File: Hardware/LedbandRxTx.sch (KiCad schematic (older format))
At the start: 74 parts, among them Q1 LED_RGB 5050, SW1 BUTTON, SW2 BUTTON, SW3 BUTTON, SW4 BUTTON, SW5 SWITCH, SW6 DIPx4

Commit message: PCB routing started. Antenna under construction
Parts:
- removed SW5: SWITCH, BtnsSwitches:SW_SS9, symbol SWITCH
- added SW5: SWITCH_H, symbol SWITCH_H
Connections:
- net +BATT: now also SW5.1
- net BAT_IN: now also SW5.2
- net GND: now also SW5.H
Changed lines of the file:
@@
 Entry Wire Line
 	6350 3100 6450 3200
-$Comp
-L SWITCH SW5
-U 1 1 5528A9A9
-P 3800 10300
-F 0 "SW5" H 3550 10550 60  0000 C CNN
-F 1 "SWITCH" H 3900 10550 60  0000 C CNN
-F 2 "BtnsSwitches:SW_SS9" H 3800 10300 60  0001 C CNN
-F 3 "" H 3800 10300 60  0000 C CNN
-	1    3800 10300
-	1    0    0    -1
-$EndComp
 NoConn ~ 4050 10200
 Text Label 2650 2000 0    60   ~ 0
@@
 Wire Wire Line
 	2100 10050 2100 9600
+$Comp
+L SWITCH_H SW5
+U 1 1 55E2F23F
+P 3800 10300
+F 0 "SW5" H 3550 10550 60  0000 C CNN
+F 1 "SWITCH_H" H 3900 10550 60  0000 C CNN
+F 2 "" H 3800 10300 60  0000 C CNN
+F 3 "" H 3800 10300 60  0000 C CNN
+	1    3800 10300
+	1    0    0    -1
+$EndComp
+$Comp
+L GND #PWR?
+U 1 1 55E2F354
+P 3750 10600
+F 0 "#PWR?" H 3840 10580 30  0001 C CNN
+F 1 "GND" H 3750 10520 30  0001 C CNN
+F 2 "" H 3750 10600 60  0001 C CNN
+F 3 "" H 3750 10600 60  0001 C CNN
+	1    3750 10600
+	1    0    0    -1
+$EndComp
+Wire Wire Line
+	3750 10500 3750 10600
 $EndSCHEMATC

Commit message: + PCB is ready, sent to production
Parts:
- removed XL5: CONN_2, Connectors:TermiBlockHeader_508_x2_R, symbol CONN_2
- added R10, R11: 100k, Resistors:RES_0603, symbol R
- added XL5: CONN_3, Connectors:TermiBlockHeader_508_x3_R, symbol CONN_3
- ANT1: footprint Radio:ANT_868_MEANDER_SALEM -> Radio:ANT_INVF_LEDBANDRXTX
- SW5: footprint (none) -> BtnsSwitches:SW_SS9
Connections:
- net +BATT: now also R10.1
- net Ch1_OUT: now also XL5.1 (P1)
- net GND: now also R11.2, XL5.2 (PM)
- net DataIn: now reaches DD1.10 (ADC0/T2C1ETR/WKUP/PA0)
- net DataIn: now also XL5.3
- net BatMeas: now reaches DD1.11 (ADC1/T2C2/PA1)
- net BatMeas: now also R10.2, R11.1
- no-connect marks 15 -> 13
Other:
- note added: "For WS2812-based band"
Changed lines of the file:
@@
 Text Notes 1900 3050 2    60   ~ 0
 Just\nPins
-NoConn ~ 5750 1700
 $Comp
 L GND #PWR027
@@
 F 0 "ANT1" H 13950 2150 60  0000 C CNN
 F 1 "ANT_PCB_MONO_2PIN" H 14300 2050 60  0000 C CNN
-F 2 "Radio:ANT_868_MEANDER_SALEM" H 14150 1900 60  0001 C CNN
+F 2 "Radio:ANT_INVF_LEDBANDRXTX" H 14150 1900 60  0001 C CNN
 F 3 "" H 14150 1900 60  0000 C CNN
 	1    14150 1900
@@
 L GND #PWR052
 U 1 1 55E1F205
-P 15300 6800
-F 0 "#PWR052" H 15390 6780 30  0001 C CNN
-F 1 "GND" H 15300 6720 30  0001 C CNN
-F 2 "" H 15300 6800 60  0001 C CNN
-F 3 "" H 15300 6800 60  0001 C CNN
-	1    15300 6800
-	1    0    0    -1
+P 15200 6600
+F 0 "#PWR052" H 15290 6580 30  0001 C CNN
+F 1 "GND" H 15200 6520 30  0001 C CNN
+F 2 "" H 15200 6600 60  0001 C CNN
+F 3 "" H 15200 6600 60  0001 C CNN
+	1    15200 6600
+	0    1    1    0
 $EndComp
 $Comp
@@
 	12150 6300 12650 6300
 Wire Wire Line
-	15300 6700 15300 6800
-Wire Wire Line
 	1600 7050 1600 7100
 Wire Wire Line
@@
 Wire Wire Line
 	2500 1800 3100 1800
-$Comp
-L CONN_2 XL5
-U 1 1 55E2515A
-P 15500 6600
-F 0 "XL5" V 15450 6600 40  0000 C CNN
-F 1 "CONN_2" V 15550 6600 40  0000 C CNN
-F 2 "Connectors:TermiBlockHeader_508_x2_R" H 15500 6600 60  0001 C CNN
-F 3 "" H 15500 6600 60  0000 C CNN
-	1    15500 6600
-	1    0    0    -1
-$EndComp
 $Comp
 L BUTTON SW2
@@
 	2900 9750 2900 9850
 NoConn ~ 3200 9450
-NoConn ~ 5750 1600
 $Comp
 L BATx3 BAT1
@@
 F 0 "SW5" H 3550 10550 60  0000 C CNN
 F 1 "SWITCH_H" H 3900 10550 60  0000 C CNN
-F 2 "" H 3800 10300 60  0000 C CNN
+F 2 "BtnsSwitches:SW_SS9" H 3800 10300 60  0001 C CNN
 F 3 "" H 3800 10300 60  0000 C CNN
 	1    3800 10300
@@
 $EndComp
 $Comp
-L GND #PWR?
+L GND #PWR061
 U 1 1 55E2F354
 P 3750 10600
-F 0 "#PWR?" H 3840 10580 30  0001 C CNN
+F 0 "#PWR061" H 3840 10580 30  0001 C CNN
 F 1 "GND" H 3750 10520 30  0001 C CNN
 F 2 "" H 3750 10600 60  0001 C CNN
@@
 Wire Wire Line
 	3750 10500 3750 10600
+$Comp
+L R R10
+U 1 1 55E35BFC
+P 4600 8700
+F 0 "R10" V 4680 8550 50  0000 C CNN
+F 1 "100k" V 4600 8700 50  0000 C CNN
+F 2 "Resistors:RES_0603" V 4680 8800 28  0000 C CNN
+F 3 "" H 4600 8700 60  0000 C CNN
+	1    4600 8700
+	1    0    0    -1
+$EndComp
+$Comp
+L R R11
+U 1 1 55E36201
+P 4600 9400
+F 0 "R11" V 4680 9250 50  0000 C CNN
+F 1 "100k" V 4600 9400 50  0000 C CNN
+F 2 "Resistors:RES_0603" V 4680 9500 28  0000 C CNN
+F 3 "" H 4600 9400 60  0000 C CNN
+	1    4600 9400
+	1    0    0    -1
+$EndComp
+$Comp
+L +BATT #PWR062
+U 1 1 55E36393
+P 4600 8350
+F 0 "#PWR062" H 4600 8310 30  0001 C CNN
+F 1 "+BATT" H 4680 8380 30  0000 C CNN
+F 2 "" H 4600 8350 60  0000 C CNN
+F 3 "" H 4600 8350 60  0000 C CNN
+	1    4600 8350
+	0    -1   -1   0
+$EndComp
+Wire Wire Line
+	4600 8350 4600 8450
+Wire Wire Line
+	4600 8950 4600 9150
+$Comp
+L GND #PWR063
+U 1 1 55E36A14
+P 4600 9750
+F 0 "#PWR063" H 4690 9730 30  0001 C CNN
+F 1 "GND" H 4600 9670 30  0001 C CNN
+F 2 "" H 4600 9750 60  0001 C CNN
+F 3 "" H 4600 9750 60  0001 C CNN
+	1    4600 9750
+	1    0    0    -1
+$EndComp
+Wire Wire Line
+	4600 9650 4600 9750
+Wire Wire Line
+	4600 9050 4750 9050
+Connection ~ 4600 9050
+Text Label 4750 9050 0    60   ~ 0
+BatMeas
+Text Label 5850 1700 0    60   ~ 0
+BatMeas
+Wire Wire Line
+	5750 1700 5850 1700
+Text Label 5850 1600 0    60   ~ 0
+DataIn
+Wire Wire Line
+	5850 1600 5750 1600
+Text Label 14900 6800 0    60   ~ 0
+DataIn
+$Comp
+L CONN_3 XL5
+U 1 1 55E38B15
+P 15500 6600
+F 0 "XL5" V 15450 6600 40  0000 C CNN
+F 1 "CONN_3" V 15550 6600 40  0000 C CNN
+F 2 "Connectors:TermiBlockHeader_508_x3_R" H 15500 6600 60  0001 C CNN
+F 3 "" H 15500 6600 60  0000 C CNN
+	1    15500 6600
+	-1   0    0    -1
+$EndComp
+Wire Wire Line
+	15200 6600 15300 6600
+Wire Wire Line
+	14900 6800 15200 6800
+Wire Wire Line
+	15200 6800 15200 6700
+Wire Wire Line
+	15200 6700 15300 6700
+Text Notes 14550 6950 0    60   ~ 0
+For WS2812-based band
 $EndSCHEMATC

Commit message: + Radio works + Radio matched
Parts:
- C26: value 1.5pF -> 3.3pF
- C28: value DoNotMount -> 3.9pF
- L3: value 5.6nH -> 15nH
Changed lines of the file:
@@
 P 12850 2350
 F 0 "C26" H 12900 2450 50  0000 L CNN
-F 1 "1.5pF" H 12900 2250 50  0000 L CNN
+F 1 "3.3pF" H 12900 2250 50  0000 L CNN
 F 2 "Capacitors:CAP_0402" H 12850 2350 60  0001 C CNN
 F 3 "" H 12850 2350 60  0001 C CNN
@@
 P 13200 1850
 F 0 "L3" V 13100 1710 40  0000 C CNN
-F 1 "5.6nH" V 13100 1850 40  0000 C CNN
+F 1 "15nH" V 13100 1850 40  0000 C CNN
 F 2 "Inductors:IND_0402" V 13260 1860 40  0000 C CNN
 F 3 "~" H 13200 1850 60  0000 C CNN
@@
 P 13550 2350
 F 0 "C28" H 13600 2450 50  0000 L CNN
-F 1 "DoNotMount" H 13600 2250 50  0000 L CNN
+F 1 "3.9pF" H 13600 2250 50  0000 L CNN
 F 2 "Capacitors:CAP_0402" H 13550 2350 60  0001 C CNN
 F 3 "" H 13550 2350 60  0001 C CNN

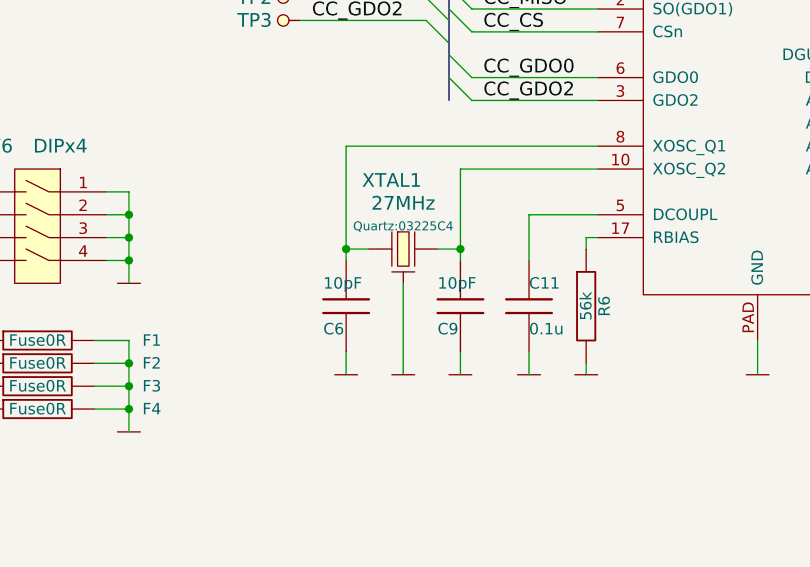
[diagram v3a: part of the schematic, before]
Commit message: * Quartz capacitors changed * Channel moved to 0 (868) from 180 (944)
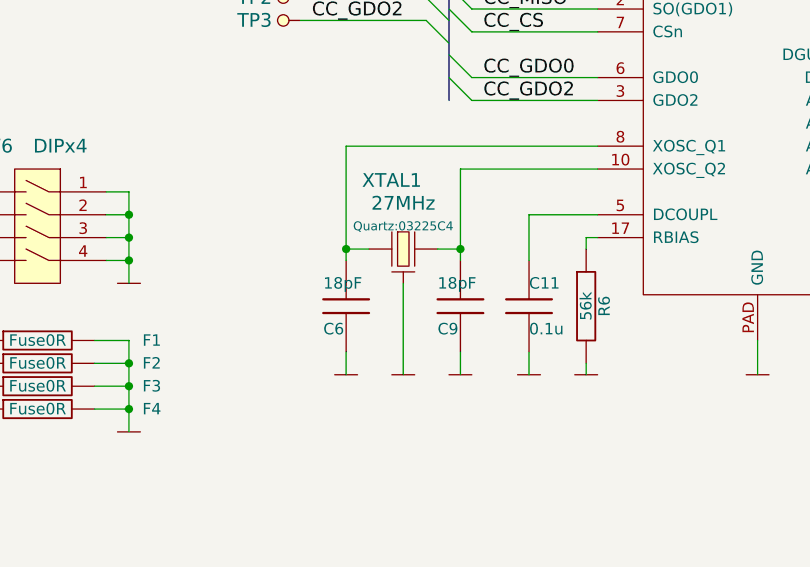
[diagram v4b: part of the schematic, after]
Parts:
- C6, C9: value 10pF -> 18pF
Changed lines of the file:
@@
 P 9000 3350
 F 0 "C9" H 8900 3250 50  0000 L CNN
-F 1 "10pF" H 8900 3450 50  0000 L CNN
+F 1 "18pF" H 8900 3450 50  0000 L CNN
 F 2 "Capacitors:CAP_0603" V 9100 3200 28  0001 C BNN
 F 3 "" H 9000 3350 60  0001 C CNN
@@
 P 8500 3350
 F 0 "C6" H 8400 3250 50  0000 L CNN
-F 1 "10pF" H 8400 3450 50  0000 L CNN
+F 1 "18pF" H 8400 3450 50  0000 L CNN
 F 2 "Capacitors:CAP_0603" V 8600 3200 28  0001 C BNN
 F 3 "" H 8500 3350 60  0001 C CNN

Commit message: RC
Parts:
- TP1, TP2, TP3: symbol TESTPOINT -> TESTPOINT-RESCUE-LedbandRxTx
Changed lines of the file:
@@
 EESchema Schematic File Version 2
+LIBS:LedbandRxTx-rescue
 LIBS:pcb_details
 LIBS:power
@@
 $EndDescr
 $Comp
-L TESTPOINT TP1
+L TESTPOINT-RESCUE-LedbandRxTx TP1
 U 1 1 551801BB
 P 3000 3300
@@
 $EndComp
 $Comp
-L TESTPOINT TP2
+L TESTPOINT-RESCUE-LedbandRxTx TP2
 U 1 1 5519A948
 P 8300 2000
@@
 $EndComp
 $Comp
-L TESTPOINT TP3
+L TESTPOINT-RESCUE-LedbandRxTx TP3
 U 1 1 5519A94F
 P 8300 2100
